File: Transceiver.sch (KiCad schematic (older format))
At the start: 29 parts, among them U2 CC1125, U3 BALF-112X-02D3, U4 SKY13372-467LF, X1 KT2520K40000DAW18TAS

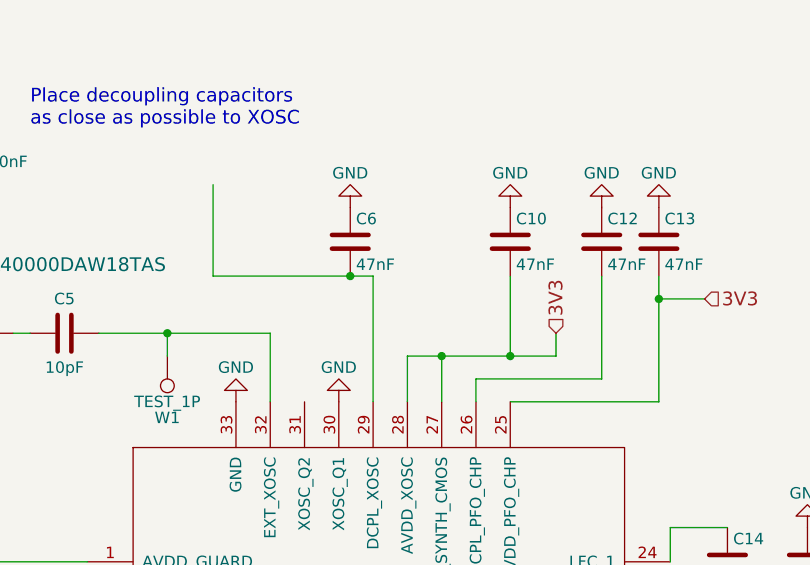
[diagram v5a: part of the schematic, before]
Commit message: Checked changes from botched commit
-R5 and R6 are gone as desired
-C4 changed from 10 nF to 100 nF looks good
-Split up nets between pins 27 and 28 so each have their own dedicated
capacitor
-Added C9 to pin 28 and forward annotated it into the layout
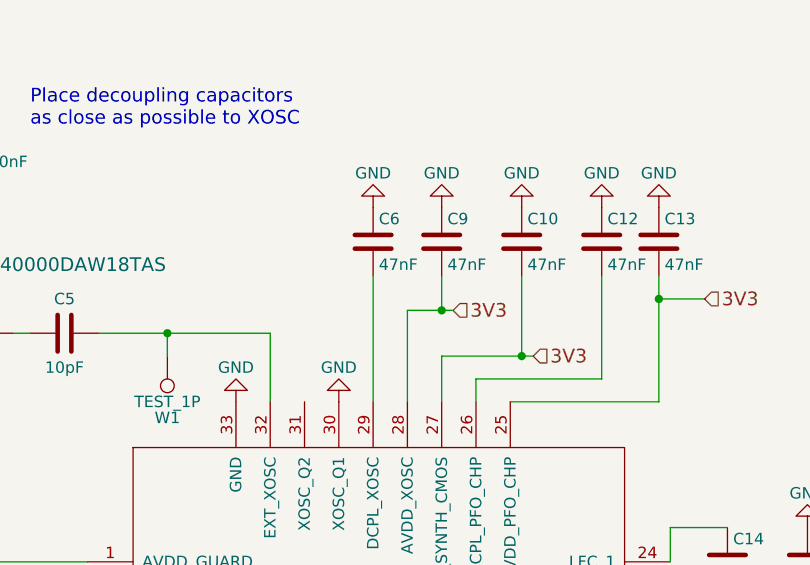
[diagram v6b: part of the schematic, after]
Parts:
- added C9: 47nF, Capacitors_SMD:C_0402, symbol C
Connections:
- net 3V3: now also C9.2
- net GND: now also C9.1
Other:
- moved on the sheet: C10, C6
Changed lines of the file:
@@
 EESchema Schematic File Version 2
+LIBS:SFUSat-Radio-rescue
 LIBS:power
 LIBS:device
@@
 $EndComp
 $Comp
-L GND #PWR06
+L GND #PWR6
 U 1 1 5821C822
 P 750 3000
-F 0 "#PWR06" H 750 2750 50  0001 C CNN
+F 0 "#PWR6" H 750 2750 50  0001 C CNN
 F 1 "GND" H 750 2850 50  0000 C CNN
 F 2 "" H 750 3000 50  0000 C CNN
@@
 $EndComp
 $Comp
-L GND #PWR07
+L GND #PWR7
 U 1 1 5821C828
 P 750 3600
-F 0 "#PWR07" H 750 3350 50  0001 C CNN
+F 0 "#PWR7" H 750 3350 50  0001 C CNN
 F 1 "GND" H 750 3450 50  0000 C CNN
 F 2 "" H 750 3600 50  0000 C CNN
@@
 $EndComp
 $Comp
-L GND #PWR08
+L GND #PWR8
 U 1 1 5821C82E
 P 750 4050
-F 0 "#PWR08" H 750 3800 50  0001 C CNN
+F 0 "#PWR8" H 750 3800 50  0001 C CNN
 F 1 "GND" H 750 3900 50  0000 C CNN
 F 2 "" H 750 4050 50  0000 C CNN
@@
 L C C10
 U 1 1 5821C842
-P 3650 1600
-F 0 "C10" H 3675 1700 50  0000 L CNN
-F 1 "47nF" H 3675 1500 50  0000 L CNN
-F 2 "Capacitors_SMD:C_0402" H 3688 1450 50  0001 C CNN
-F 3 "" H 3650 1600 50  0000 C CNN
-	1    3650 1600
-	1    0    0    -1
-$EndComp
-$Comp
-L GND #PWR09
+P 3700 1600
+F 0 "C10" H 3725 1700 50  0000 L CNN
+F 1 "47nF" H 3725 1500 50  0000 L CNN
+F 2 "Capacitors_SMD:C_0402" H 3738 1450 50  0001 C CNN
+F 3 "" H 3700 1600 50  0000 C CNN
+	1    3700 1600
+	1    0    0    -1
+$EndComp
+$Comp
+L GND #PWR16
 U 1 1 5821C849
-P 3650 1450
-F 0 "#PWR09" H 3650 1200 50  0001 C CNN
-F 1 "GND" H 3650 1300 50  0000 C CNN
-F 2 "" H 3650 1450 50  0000 C CNN
-F 3 "" H 3650 1450 50  0000 C CNN
-	1    3650 1450
+P 3700 1450
+F 0 "#PWR16" H 3700 1200 50  0001 C CNN
+F 1 "GND" H 3700 1300 50  0000 C CNN
+F 2 "" H 3700 1450 50  0000 C CNN
+F 3 "" H 3700 1450 50  0000 C CNN
+	1    3700 1450
 	-1   0    0    1
 $EndComp
@@
 $EndComp
 $Comp
-L GND #PWR010
+L GND #PWR19
 U 1 1 5821C856
 P 4050 1450
-F 0 "#PWR010" H 4050 1200 50  0001 C CNN
+F 0 "#PWR19" H 4050 1200 50  0001 C CNN
 F 1 "GND" H 4050 1300 50  0000 C CNN
 F 2 "" H 4050 1450 50  0000 C CNN
@@
 $EndComp
 $Comp
-L GND #PWR011
+L GND #PWR20
 U 1 1 5821C863
 P 4300 1450
-F 0 "#PWR011" H 4300 1200 50  0001 C CNN
+F 0 "#PWR20" H 4300 1200 50  0001 C CNN
 F 1 "GND" H 4300 1300 50  0000 C CNN
 F 2 "" H 4300 1450 50  0000 C CNN
@@
 L C C6
 U 1 1 5821C869
-P 2950 1600
-F 0 "C6" H 2975 1700 50  0000 L CNN
-F 1 "47nF" H 2975 1500 50  0000 L CNN
-F 2 "Capacitors_SMD:C_0402" H 2988 1450 50  0001 C CNN
-F 3 "" H 2950 1600 50  0000 C CNN
-	1    2950 1600
-	1    0    0    -1
-$EndComp
-$Comp
-L GND #PWR012
+P 3050 1600
+F 0 "C6" H 3075 1700 50  0000 L CNN
+F 1 "47nF" H 3075 1500 50  0000 L CNN
+F 2 "Capacitors_SMD:C_0402" H 3088 1450 50  0001 C CNN
+F 3 "" H 3050 1600 50  0000 C CNN
+	1    3050 1600
+	1    0    0    -1
+$EndComp
+$Comp
+L GND #PWR14
 U 1 1 5821C870
-P 2950 1450
-F 0 "#PWR012" H 2950 1200 50  0001 C CNN
-F 1 "GND" H 2950 1300 50  0000 C CNN
-F 2 "" H 2950 1450 50  0000 C CNN
-F 3 "" H 2950 1450 50  0000 C CNN
-	1    2950 1450
+P 3050 1450
+F 0 "#PWR14" H 3050 1200 50  0001 C CNN
+F 1 "GND" H 3050 1300 50  0000 C CNN
+F 2 "" H 3050 1450 50  0000 C CNN
+F 3 "" H 3050 1450 50  0000 C CNN
+	1    3050 1450
 	-1   0    0    1
 $EndComp
@@
 $EndComp
 $Comp
-L GND #PWR013
+L GND #PWR13
 U 1 1 5821C88A
 P 3000 5400
-F 0 "#PWR013" H 3000 5150 50  0001 C CNN
+F 0 "#PWR13" H 3000 5150 50  0001 C CNN
 F 1 "GND" H 3000 5250 50  0000 C CNN
 F 2 "" H 3000 5400 50  0000 C CNN
@@
 $EndComp
 $Comp
-L GND #PWR014
+L GND #PWR18
 U 1 1 5821C897
 P 4000 5400
-F 0 "#PWR014" H 4000 5150 50  0001 C CNN
+F 0 "#PWR18" H 4000 5150 50  0001 C CNN
 F 1 "GND" H 4000 5250 50  0000 C CNN
 F 2 "" H 4000 5400 50  0000 C CNN
@@
 $EndComp
 $Comp
-L GND #PWR015
+L GND #PWR17
 U 1 1 5821C8A8
 P 3700 5400
-F 0 "#PWR015" H 3700 5150 50  0001 C CNN
+F 0 "#PWR17" H 3700 5150 50  0001 C CNN
 F 1 "GND" H 3700 5250 50  0000 C CNN
 F 2 "" H 3700 5400 50  0000 C CNN
@@
 $EndComp
 $Comp
-L GND #PWR016
+L GND #PWR21
 U 1 1 5821C8BD
 P 4950 2850
-F 0 "#PWR016" H 4950 2600 50  0001 C CNN
+F 0 "#PWR21" H 4950 2600 50  0001 C CNN
 F 1 "GND" H 4950 2700 50  0000 C CNN
 F 2 "" H 4950 2850 50  0000 C CNN
@@
 $EndComp
 $Comp
-L GND #PWR017
+L GND #PWR22
 U 1 1 5821C8CA
 P 5450 2850
-F 0 "#PWR017" H 5450 2600 50  0001 C CNN
+F 0 "#PWR22" H 5450 2600 50  0001 C CNN
 F 1 "GND" H 5450 2700 50  0000 C CNN
 F 2 "" H 5450 2850 50  0000 C CNN
@@
 $EndComp
 $Comp
-L GND #PWR018
+L GND #PWR11
 U 1 1 5821C9D7
 P 2450 2300
-F 0 "#PWR018" H 2450 2050 50  0001 C CNN
+F 0 "#PWR11" H 2450 2050 50  0001 C CNN
 F 1 "GND" H 2450 2150 50  0000 C CNN
 F 2 "" H 2450 2300 50  0000 C CNN
@@
 $EndComp
 $Comp
-L GND #PWR019
+L GND #PWR12
 U 1 1 5821C9E6
 P 2900 2300
-F 0 "#PWR019" H 2900 2050 50  0001 C CNN
+F 0 "#PWR12" H 2900 2050 50  0001 C CNN
 F 1 "GND" H 2900 2150 50  0000 C CNN
 F 2 "" H 2900 2300 50  0000 C CNN
@@
 $EndComp
 $Comp
-L GND #PWR020
+L GND #PWR9
 U 1 1 5821C9FA
 P 1025 2600
-F 0 "#PWR020" H 1025 2350 50  0001 C CNN
+F 0 "#PWR9" H 1025 2350 50  0001 C CNN
 F 1 "GND" H 1025 2450 50  0000 C CNN
 F 2 "" H 1025 2600 50  0000 C CNN
@@
 Text HLabel 1025 900  1    60   Input ~ 0
 1V8
-Text HLabel 3850 2000 1    60   Input ~ 0
+Text HLabel 3750 2100 2    60   Input ~ 0
 3V3
 Text HLabel 4500 1850 2    60   Input ~ 0
@@
 $EndComp
 $Comp
-L GND #PWR021
+L GND #PWR23
 U 1 1 58730157
 P 7000 3650
-F 0 "#PWR021" H 7000 3400 50  0001 C CNN
+F 0 "#PWR23" H 7000 3400 50  0001 C CNN
 F 1 "GND" H 7000 3500 50  0000 C CNN
 F 2 "" H 7000 3650 50  0000 C CNN
@@
 $EndComp
 $Comp
-L GND #PWR022
+L GND #PWR24
 U 1 1 5873019B
 P 7000 3950
-F 0 "#PWR022" H 7000 3700 50  0001 C CNN
+F 0 "#PWR24" H 7000 3700 50  0001 C CNN
 F 1 "GND" H 7000 3800 50  0000 C CNN
 F 2 "" H 7000 3950 50  0000 C CNN
@@
 TX
 $Comp
-L GND #PWR023
+L GND #PWR25
 U 1 1 58748992
 P 8575 4525
-F 0 "#PWR023" H 8575 4275 50  0001 C CNN
+F 0 "#PWR25" H 8575 4275 50  0001 C CNN
 F 1 "GND" H 8575 4375 50  0000 C CNN
 F 2 "" H 8575 4525 50  0000 C CNN
@@
 $EndComp
 $Comp
-L GND #PWR024
+L GND #PWR10
 U 1 1 5873A98A
 P 1300 950
-F 0 "#PWR024" H 1300 700 50  0001 C CNN
+F 0 "#PWR10" H 1300 700 50  0001 C CNN
 F 1 "GND" H 1300 800 50  0000 C CNN
 F 2 "" H 1300 950 50  0000 C CNN
@@
 $EndComp
 $Comp
-L GND #PWR026
+L GND #PWR26
 U 1 1 5883AD14
 P 8850 3225
-F 0 "#PWR026" H 8850 2975 50  0001 C CNN
+F 0 "#PWR26" H 8850 2975 50  0001 C CNN
 F 1 "GND" H 8850 3075 50  0000 C CNN
 F 2 "" H 8850 3225 50  0000 C CNN
@@
 	3350 2300 3350 2100
 Wire Wire Line
-	3200 2100 3850 2100
-Wire Wire Line
-	3650 2100 3650 1750
-Wire Wire Line
-	3850 2100 3850 2000
-Connection ~ 3650 2100
+	3700 2100 3700 1750
 Wire Wire Line
 	3050 1750 3050 2300
@@
 Wire Wire Line
 	1300 1000 1300 950
-Connection ~ 2950 1750
 Wire Wire Line
 	1475 2000 1550 2000
@@
 Wire Wire Line
 	4000 4700 4000 5100
-Wire Wire Line
-	2350 1750 3050 1750
-Wire Wire Line
-	2350 1350 2350 1750
 Wire Wire Line
 	7800 3200 8475 3200
@@
 Connection ~ 2150 2000
 Wire Wire Line
-	3200 2300 3200 2100
-Connection ~ 3350 2100
+	3200 1900 3200 2300
 Wire Wire Line
 	8575 2800 8575 3200
@@
 	1300 1425 1025 1425
 Connection ~ 1025 1425
+$Comp
+L C C9
+U 1 1 588558AB
+P 3350 1600
+F 0 "C9" H 3375 1700 50  0000 L CNN
+F 1 "47nF" H 3375 1500 50  0000 L CNN
+F 2 "Capacitors_SMD:C_0402" H 3388 1450 50  0001 C CNN
+F 3 "" H 3350 1600 50  0000 C CNN
+	1    3350 1600
+	1    0    0    -1
+$EndComp
+$Comp
+L GND #PWR15
+U 1 1 588558B1
+P 3350 1450
+F 0 "#PWR15" H 3350 1200 50  0001 C CNN
+F 1 "GND" H 3350 1300 50  0000 C CNN
+F 2 "" H 3350 1450 50  0000 C CNN
+F 3 "" H 3350 1450 50  0000 C CNN
+	1    3350 1450
+	-1   0    0    1
+$EndComp
+Wire Wire Line
+	3350 1750 3350 1900
+Wire Wire Line
+	3200 1900 3400 1900
+Text HLabel 3400 1900 2    60   Input ~ 0
+3V3
+Connection ~ 3350 1900
+Wire Wire Line
+	3350 2100 3750 2100
+Connection ~ 3700 2100
 $EndSCHEMATC

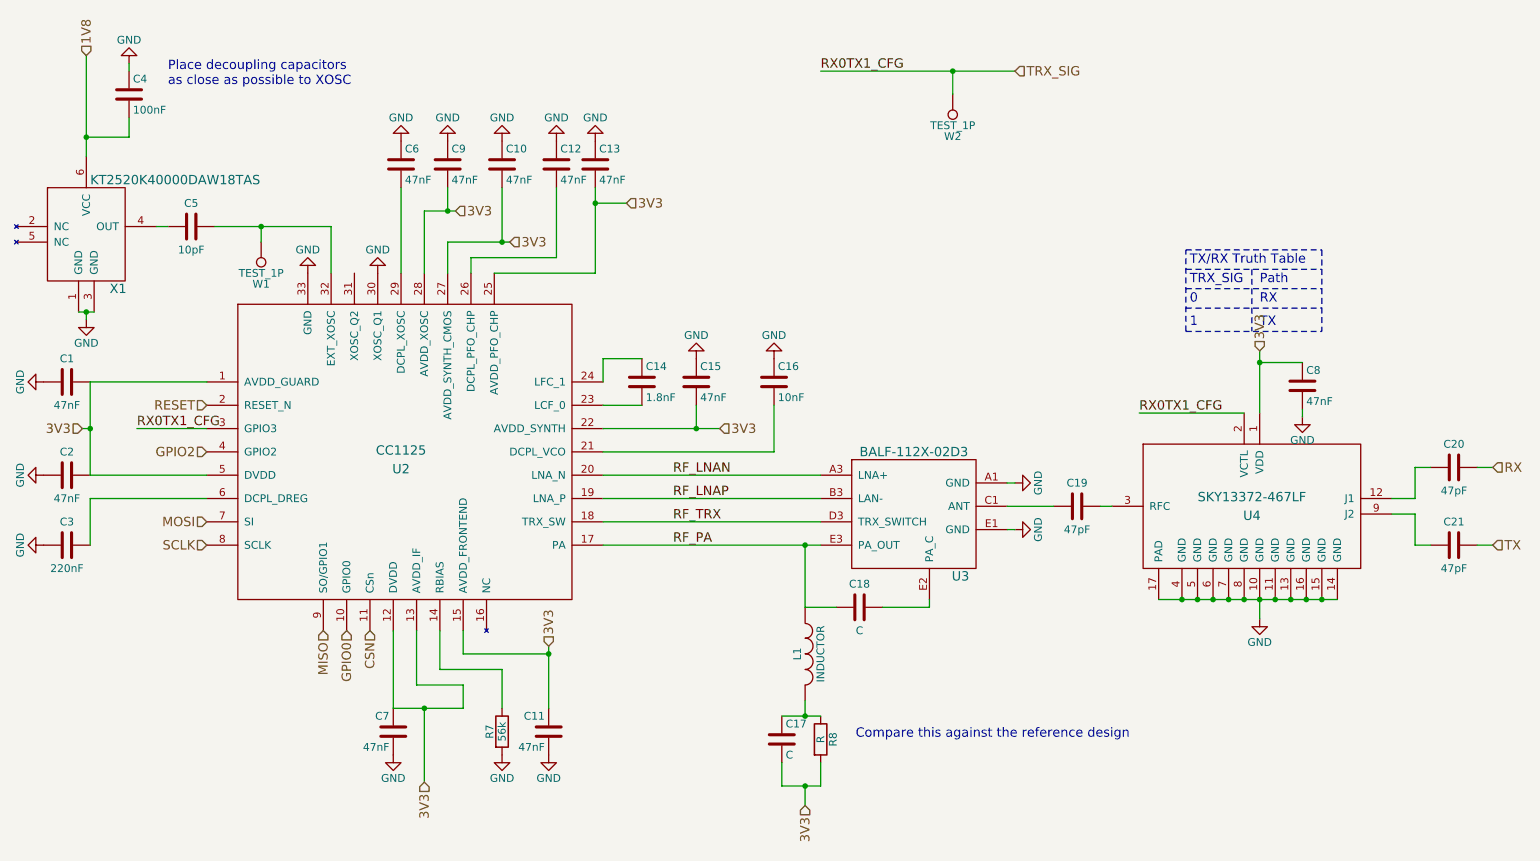
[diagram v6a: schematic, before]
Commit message: added all the gnd and pwr planes
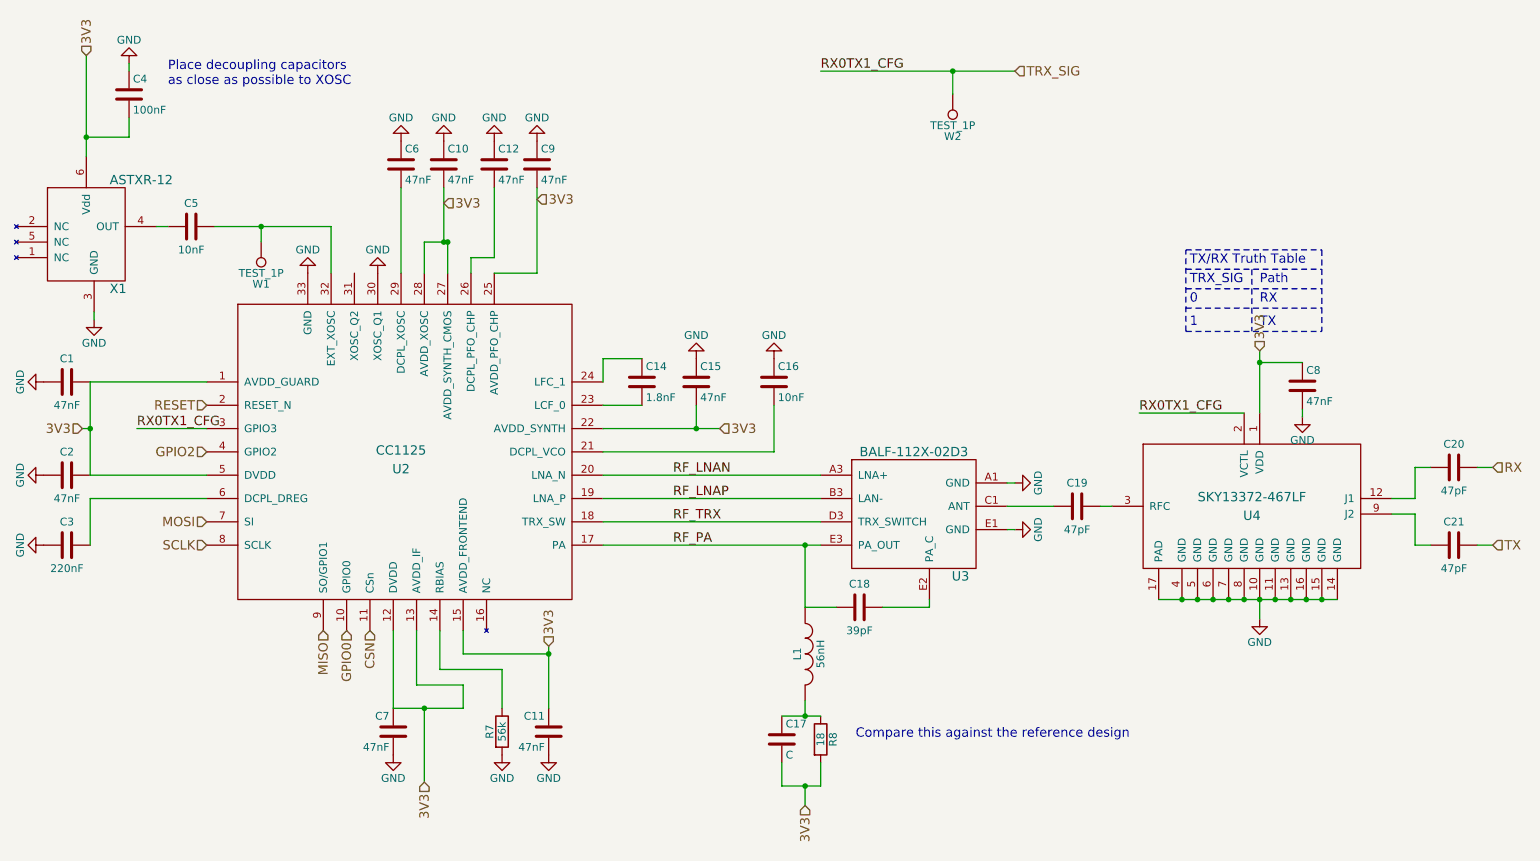
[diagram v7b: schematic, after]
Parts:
- removed C13: 47nF, Capacitors_SMD:C_0402, symbol C
- removed X1: KT2520K40000DAW18TAS, SFUSat-Radio:DFN-6, symbol KT2520K40000DAW18TAS
- added X1: ASTXR-12, SFUSat-Radio:ASTXR-12, symbol ASTXR-12
- C18: value C -> 39pF
- C5: value 10pF -> 10nF
- L1: value INDUCTOR -> 56nH
- R8: value R -> 18
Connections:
- net 1V8 is gone; now on net 3V3: C4.2
- net 3V3: now also X1.6 (Vdd)
- net GND: now also X1.3 (GND)
- net at C5.2: now also X1.4 (OUT)
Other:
- moved on the sheet: C10, C12
